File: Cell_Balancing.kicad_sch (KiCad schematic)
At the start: 29 parts, among them IC6 BQ7694204PFBR, J6 Conn_01x06, Q10 MMBT5551LT1G

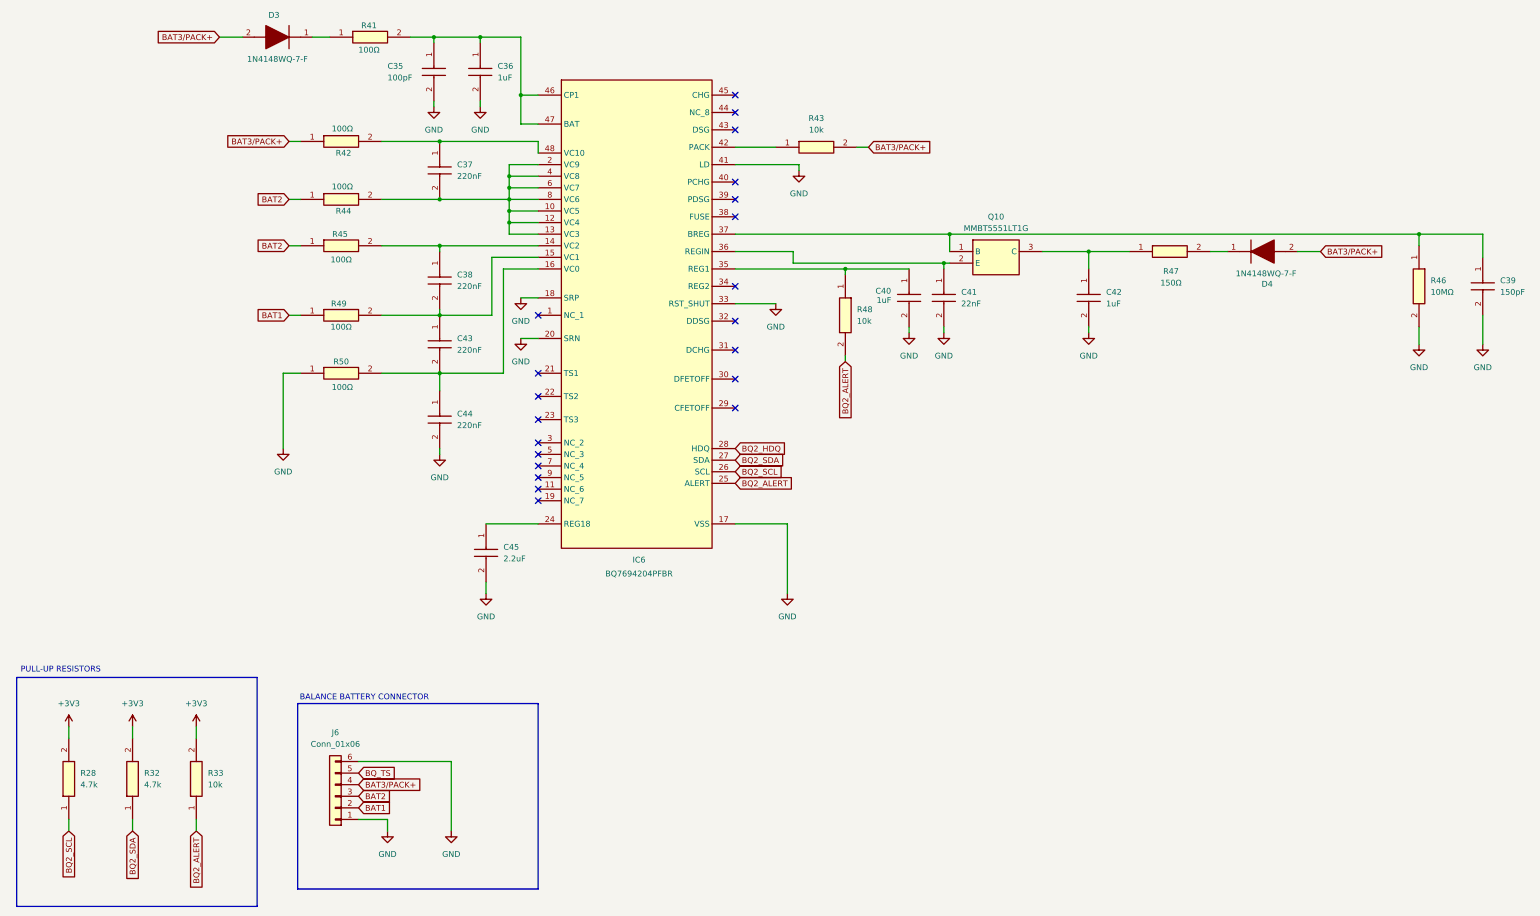
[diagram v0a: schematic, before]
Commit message: Added Ratings+Net Labels+First Layout Try+Calculations Excel
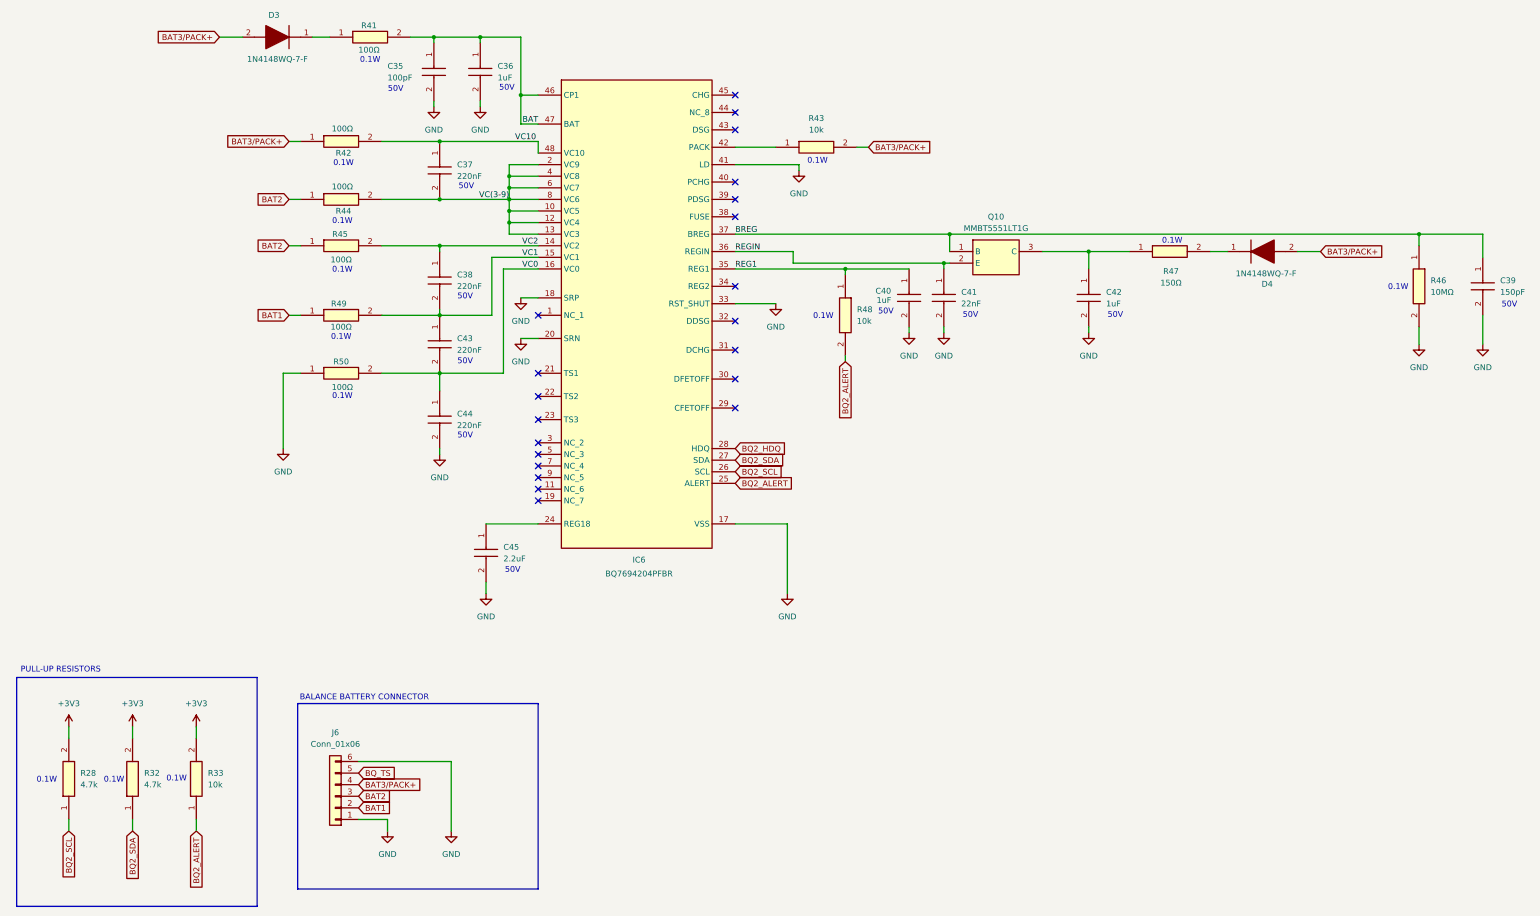
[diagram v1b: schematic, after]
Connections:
- net VC0: now reaches C43.2, C44.1, IC6.16 (VC0), R50.2
- net VC(3-9): now reaches C37.2, IC6.10 (VC5), IC6.12 (VC4), IC6.13 (VC3), IC6.2 (VC9), IC6.4 (VC8), IC6.6 (VC7), IC6.8 (VC6), R44.2
- net BREG: now reaches C39.1, IC6.37 (BREG), Q10.1 (B), R46.1
- net VC2: now reaches C38.1, IC6.14 (VC2), R45.2
- net VC1: now reaches C38.2, C43.1, IC6.15 (VC1), R49.2
- net REGIN: now reaches C41.1, IC6.36 (REGIN), Q10.2 (E)
- net VC10: now reaches C37.1, IC6.48 (VC10), R42.2
- net BAT: now reaches C35.1, C36.1, IC6.46 (CP1), IC6.47 (BAT), R41.2
- net REG1: now reaches C40.1, IC6.35 (REG1), R48.1
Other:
- note added: "0.1W"
- note added: "50V"

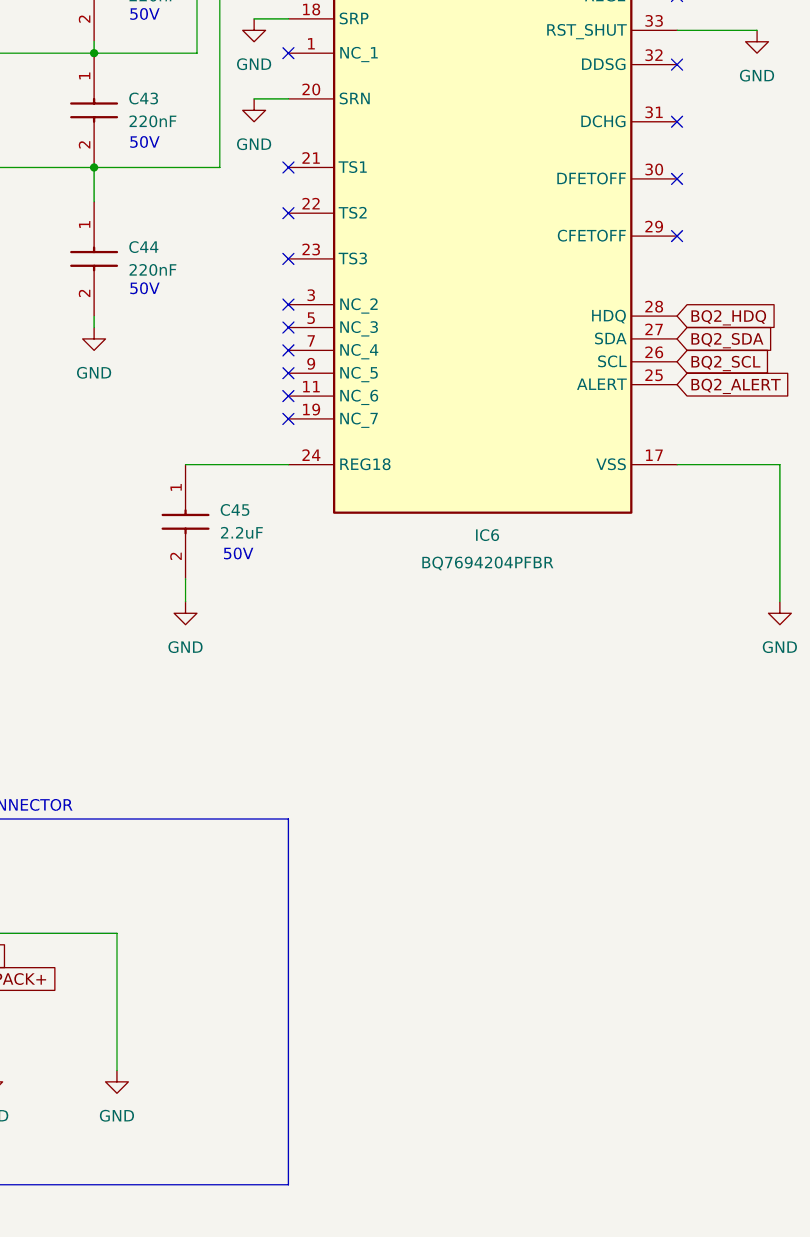
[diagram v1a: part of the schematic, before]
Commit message: Added Single-Cell Thermistor Pins
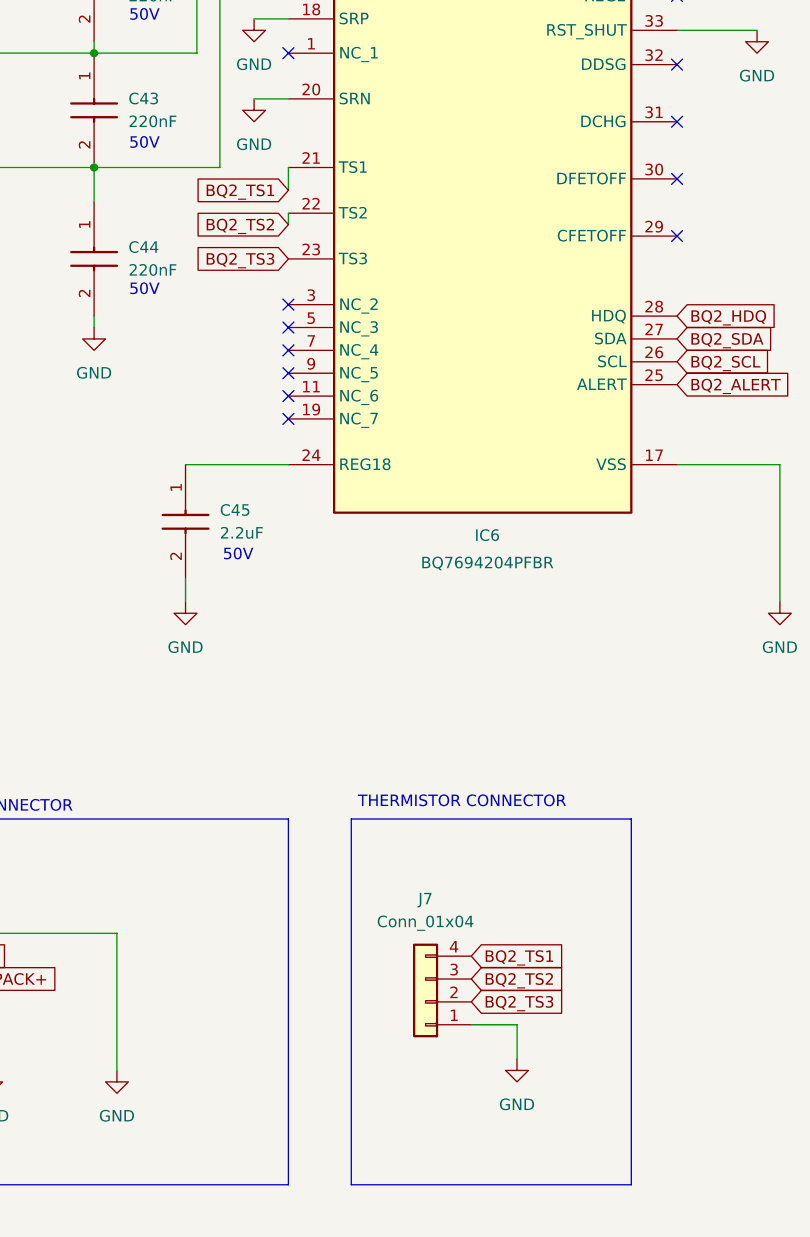
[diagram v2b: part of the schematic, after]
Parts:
- added J7: Conn_01x04, Connector_JST:JST_XH_B4B-XH-A_1x04_P2.50mm_Vertical, symbol Connector_Generic:Conn_01x04
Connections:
- net GND: now also J7.1 (Pin_1)
- net BQ2_TS1: now reaches IC6.21 (TS1)
- net BQ2_TS1: now also J7.4 (Pin_4)
- net BQ2_TS2: now reaches IC6.22 (TS2)
- net BQ2_TS2: now also J7.3 (Pin_3)
- net BQ2_TS3: now reaches IC6.23 (TS3)
- net BQ2_TS3: now also J7.2 (Pin_2)
- no-connect marks 21 -> 18
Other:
- note added: "THERMISTOR CONNECTOR"

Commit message: First Changes
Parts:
- removed R28, R32: 4.7k, RC0603FR-074K7L:RESC1608X55N, symbol RC0603FR-074K7L:RC0603FR-074K7L
- removed R48: 10k, RC0603FR-0710KL:RESC1608X55N, symbol RC0603FR-0710KL:RC0603FR-0710KL
- added R28: 10k, RC0603FR-0710KL:RESC1608X55N, symbol RC0603FR-0710KL:RC0603FR-0710KL
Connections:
- net +3V3: now also R28.1
- net BQ2_CS: now reaches IC6.29 (CFETOFF)
- net BQ2_CS: now also R28.2
- net BQ2_HDQ renamed BQ2_MOSI
- net BQ2_SCL renamed BQ2_SCLK
- net BQ2_SDA renamed BQ2_MISO
- no-connect marks 18 -> 17
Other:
- moved on the sheet: C40, R33

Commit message: TS fixed + Small Changes
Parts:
- removed R45: 100Ω, RC0603FR-07100RL:RESC1608X55N, symbol RC0603FR-07100RL:RC0603FR-07100RL
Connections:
- net VC2 is gone; now on net VC(3-9): C38.1, IC6.14 (VC2)
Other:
- moved on the sheet: R44
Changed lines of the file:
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@@
 	(text "0.1W"
 		(exclude_from_sim no)
-		(at 92.964 119.634 0)
-		(effects
-			(font
-				(size 1.27 1.27)
-				(color 255 4 0 1)
-			)
-		)
-	)
-	(text "0.1W"
-		(exclude_from_sim no)
 		(at 92.964 147.32 0)
 		(effects
@@
 	(text "0.1W"
 		(exclude_from_sim no)
-		(at 92.964 108.966 0)
+		(at 92.71 113.792 0)
 		(effects
 			(font
@@
 	)
 	(junction
+		(at 114.3 109.22)
+		(diameter 0)
+		(color 0 0 0 0)
+	)
+	(junction
 		(at 226.06 111.76)
 		(diameter 0)
@@
 	)
 	(junction
-		(at 123.19 68.58)
+		(at 114.3 114.3)
 		(diameter 0)
 		(color 0 0 0 0)
 	)
 	(junction
-		(at 114.3 114.3)
+		(at 123.19 68.58)
 		(diameter 0)
 		(color 0 0 0 0)
@@
 	(wire
 		(pts
-			(xy 101.6 114.3) (xy 114.3 114.3)
+			(xy 129.54 101.6) (xy 135.89 101.6)
 		)
 		(stroke
@@
 	(wire
 		(pts
-			(xy 129.54 101.6) (xy 135.89 101.6)
+			(xy 80.01 109.22) (xy 83.82 109.22)
 		)
 		(stroke
@@
 	(wire
 		(pts
-			(xy 101.6 104.14) (xy 114.3 104.14)
+			(xy 101.6 109.22) (xy 114.3 109.22)
 		)
 		(stroke
@@
 	(wire
 		(pts
-			(xy 81.28 114.3) (xy 83.82 114.3)
+			(xy 132.08 68.58) (xy 123.19 68.58)
 		)
 		(stroke
@@
 	(wire
 		(pts
-			(xy 132.08 68.58) (xy 123.19 68.58)
+			(xy 224.79 132.08) (xy 224.79 133.35)
 		)
 		(stroke
@@
 	(wire
 		(pts
-			(xy 224.79 132.08) (xy 224.79 133.35)
+			(xy 114.3 109.22) (xy 114.3 104.14)
 		)
 		(stroke
@@
 	(wire
 		(pts
-			(xy 101.6 91.44) (xy 114.3 91.44)
+			(xy 114.3 109.22) (xy 114.3 114.3)
 		)
 		(stroke
@@
 	(wire
 		(pts
-			(xy 114.3 146.05) (xy 114.3 142.24)
+			(xy 101.6 91.44) (xy 114.3 91.44)
 		)
 		(stroke
@@
 	(wire
 		(pts
-			(xy 135.89 87.63) (xy 132.08 87.63)
+			(xy 114.3 146.05) (xy 114.3 142.24)
 		)
 		(stroke
@@
 	(wire
 		(pts
-			(xy 179.07 119.38) (xy 205.74 119.38)
+			(xy 135.89 87.63) (xy 132.08 87.63)
 		)
 		(stroke
@@
 	(wire
 		(pts
-			(xy 256.54 132.08) (xy 256.54 133.35)
+			(xy 179.07 119.38) (xy 205.74 119.38)
 		)
 		(stroke
@@
 	(wire
 		(pts
-			(xy 246.38 115.57) (xy 256.54 115.57)
+			(xy 256.54 132.08) (xy 256.54 133.35)
 		)
 		(stroke
@@
 	(wire
 		(pts
-			(xy 81.28 104.14) (xy 83.82 104.14)
+			(xy 246.38 115.57) (xy 256.54 115.57)
 		)
 		(stroke
@@
 		)
 	)
-	(global_label "BAT2"
-		(shape input)
-		(at 81.28 114.3 180)
-		(fields_autoplaced yes)
-		(effects
-			(font
-				(size 1.27 1.27)
-			)
-			(justify right)
-		)
-		(property "Intersheetrefs" "${INTERSHEET_REFS}"
-			(at 73.7591 114.3 0)
-			(effects
-				(font
-					(size 1.27 1.27)
-				)
-				(justify right)
-				(hide yes)
-			)
-		)
-	)
 	(global_label "BQ2_CS"
 		(shape input)
@@
 	(global_label "BAT2"
 		(shape input)
-		(at 81.28 104.14 180)
+		(at 80.01 109.22 180)
 		(fields_autoplaced yes)
 		(effects
@@
 		)
 		(property "Intersheetrefs" "${INTERSHEET_REFS}"
-			(at 73.7591 104.14 0)
+			(at 72.4891 109.22 0)
 			(effects
 				(font
@@
 	(symbol
 		(lib_id "RC0603FR-07100RL:RC0603FR-07100RL")
-		(at 83.82 104.14 0)
+		(at 83.82 109.22 0)
 		(unit 1)
 		(exclude_from_sim no)
@@
 		(dnp no)
 		(property "Reference" "R44"
-			(at 93.218 106.68 0)
+			(at 93.218 111.76 0)
 			(effects
 				(font
@@
 		)
 		(property "Value" "100Ω"
-			(at 92.964 101.346 0)
+			(at 92.964 106.426 0)
 			(effects
 				(font
@@
 		)
 		(property "Footprint" "RC0603FR-07100RL:RESC1608X55N"
-			(at 97.79 200.33 0)
+			(at 97.79 205.41 0)
 			(effects
 				(font
@@
 		)
 		(property "Datasheet" "http://www.yageo.com/documents/recent/PYu-RC0603_51_RoHS_L_v5.pdf"
-			(at 97.79 300.33 0)
+			(at 97.79 305.41 0)
 			(effects
 				(font
@@
 		)
 		(property "Description" "Yageo RC Series Thick Film Surface Mount Resistor 0603 Case 100"
-			(at 83.82 104.14 0)
+			(at 83.82 109.22 0)
 			(effects
 				(font
@@
 		)
 		(property "Height" "0.55"
-			(at 97.79 500.33 0)
+			(at 97.79 505.41 0)
 			(effects
 				(font
@@
 		)
 		(property "Mouser Part Number" "603-RC0603FR-07100RL"
-			(at 97.79 600.33 0)
+			(at 97.79 605.41 0)
 			(effects
 				(font
@@
 		)
 		(property "Mouser Price/Stock" "https://www.mouser.co.uk/ProductDetail/YAGEO/RC0603FR-07100RL?qs=NEN%2FsE%2FLsvPIwIWKCOS4%2FA%3D%3D"
-			(at 97.79 700.33 0)
+			(at 97.79 705.41 0)
 			(effects
 				(font
@@
 		)
 		(property "Manufacturer_Name" "Yageo Group"
-			(at 97.79 800.33 0)
+			(at 97.79 805.41 0)
 			(effects
 				(font
@@
 		)
 		(property "Manufacturer_Part_Number" "RC0603FR-07100RL"
-			(at 97.79 900.33 0)
+			(at 97.79 905.41 0)
 			(effects
 				(font
@@
 					(unit 1)
 				)
-			)
-		)
-	)
-	(symbol
-		(lib_id "RC0603FR-07100RL:RC0603FR-07100RL")
-		(at 83.82 114.3 0)
-		(unit 1)
-		(exclude_from_sim no)
-		(in_bom yes)
-		(on_board yes)
-		(dnp no)
-		(property "Reference" "R45"
-			(at 92.456 111.76 0)
-			(effects
-				(font
-					(size 1.27 1.27)
-				)
-			)
-		)
-		(property "Value" "100Ω"
-			(at 92.71 117.348 0)
-			(effects
-				(font
-					(size 1.27 1.27)
-				)
-			)
-		)
-		(property "Footprint" "RC0603FR-07100RL:RESC1608X55N"
-			(at 97.79 210.49 0)
-			(effects
-				(font
-					(size 1.27 1.27)
-				)
-				(justify left top)
-				(hide yes)
-			)
-		)
-		(property "Datasheet" "http://www.yageo.com/documents/recent/PYu-RC0603_51_RoHS_L_v5.pdf"
-			(at 97.79 310.49 0)
-			(effects
-				(font
-					(size 1.27 1.27)
-				)
-				(justify left top)
-				(hide yes)
-			)
-		)
-		(property "Description" "Yageo RC Series Thick Film Surface Mount Resistor 0603 Case 100"
-			(at 83.82 114.3 0)
-			(effects
-				(font
-					(size 1.27 1.27)
-				)
-				(hide yes)
-			)
-		)
-		(property "Height" "0.55"
-			(at 97.79 510.49 0)
-			(effects
-				(font
-					(size 1.27 1.27)
-				)
-				(justify left top)
-				(hide yes)
-			)
-		)
-		(property "Mouser Part Number" "603-RC0603FR-07100RL"
-			(at 97.79 610.49 0)
-			(effects
-				(font
-					(size 1.27 1.27)
-				)
-				(justify left top)
-				(hide yes)
-			)
-		)
-		(property "Mouser Price/Stock" "https://www.mouser.co.uk/ProductDetail/YAGEO/RC0603FR-07100RL?qs=NEN%2FsE%2FLsvPIwIWKCOS4%2FA%3D%3D"
-			(at 97.79 710.49 0)
-			(effects
-				(font
-					(size 1.27 1.27)
-				)
-				(justify left top)
-				(hide yes)
-			)
-		)
-		(property "Manufacturer_Name" "Yageo Group"
-			(at 97.79 810.49 0)
-			(effects
-				(font
-					(size 1.27 1.27)
-				)
-				(justify left top)
-				(hide yes)
-			)
-		)
-		(property "Manufacturer_Part_Number" "RC0603FR-07100RL"
-			(at 97.79 910.49 0)
-			(effects
-				(font
-					(size 1.27 1.27)
-				)
-				(justify left top)
-				(hide yes)
-			)
-		)
-		(pin "2"
-		)
-		(pin "1"
-		)
-		(instances
-			(project "Lithium_Board"
-				(path "/a208389b-7ee7-48d8-95f2-b3e129849547/c4a855d5-ac6f-48c0-9386-1c7b76fc99f3"
-					(reference "R45")
-					(unit 1)
-				)
